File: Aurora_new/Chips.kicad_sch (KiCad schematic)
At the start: 89 parts, among them J1 UJ20-C-H-C-3-SMT-TR, J16 PPPC042LFBN-RC, J3 PPPC042LFBN-RC, J36 PPPC042LFBN-RC, J41 STEMMA QT, J6 DM3AT-SF-PEJM5, U1 STM32H757BITx, U13 XBP9X-DMUS-001, U14 MS5611-01BA, U2 USBLC6-2SC6, U3 TPS2121RUXR, U4 AP63203QWU-7, U5 ICM-45686, U6 ICM-42688-P, U7 BNO085, U9 MCP23017T-E_SO

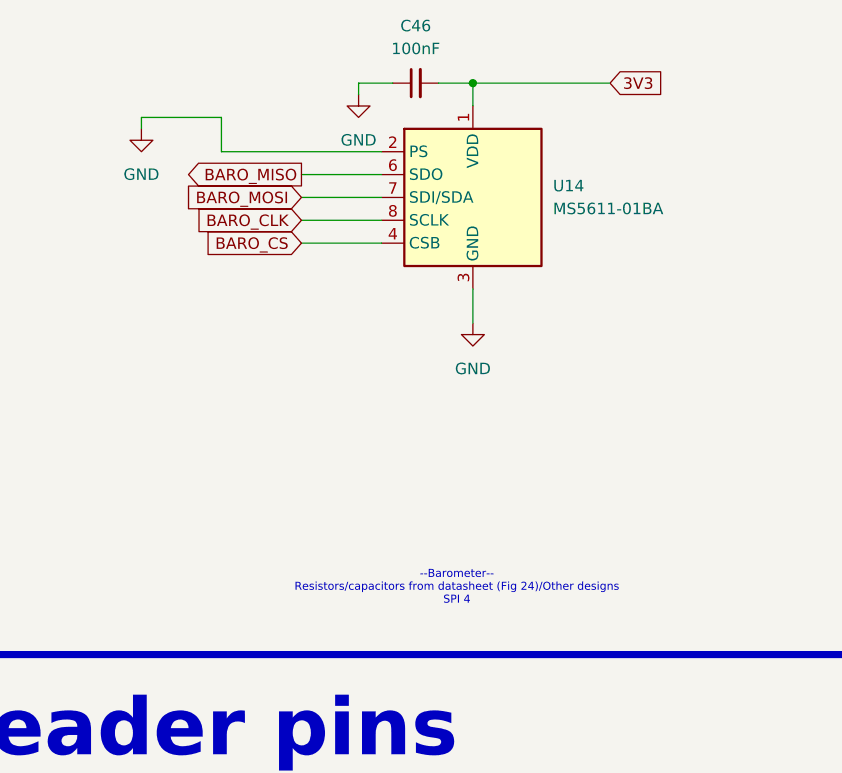
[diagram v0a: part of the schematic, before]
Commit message: PU resistor on CS for baro
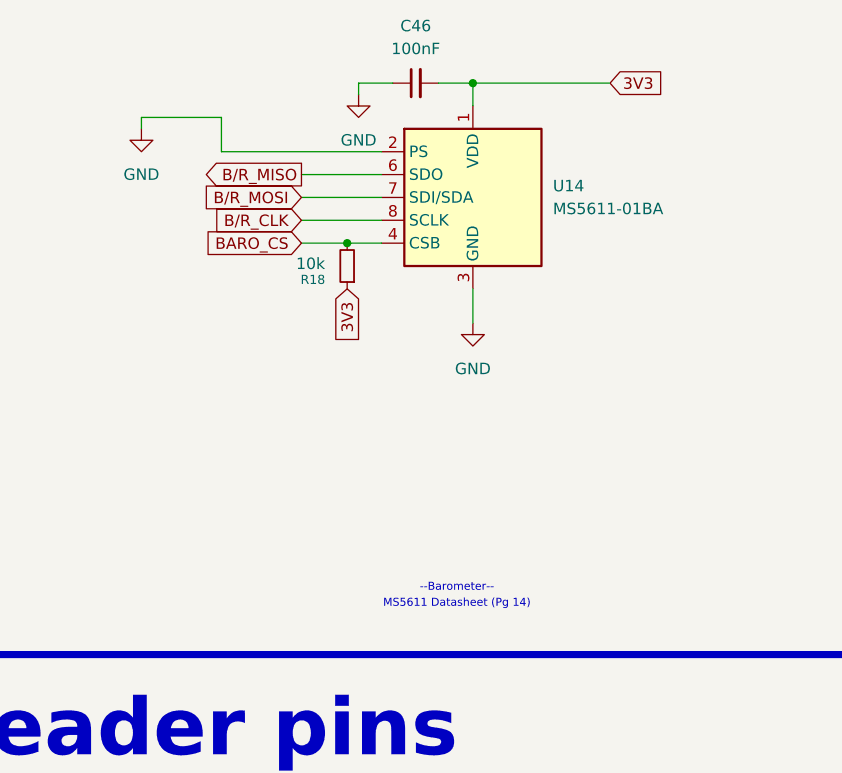
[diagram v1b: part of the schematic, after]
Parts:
- added R18: 10k, Resistor_SMD:R_0805_2012Metric, symbol Device:R_Small
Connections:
- net BARO_CLK is gone; now on net B/R_CLK: U14.8 (SCLK)
- net BARO_MISO is gone; now on net B/R_MISO: U14.6 (SDO)
- net BARO_MOSI is gone; now on net B/R_MOSI: U14.7 (SDI/SDA)
- net 3V3: now also R18.1
- net BARO_CS: now also R18.2
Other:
- note added: "--Barometer--"
- note added: "MS5611 Datasheet (Pg 14)"
- note removed: "--Barometer-- Resistors/capacitors from datasheet (Fig 24)/Other designs SPI 4"
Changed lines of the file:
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@@
 		)
 	)
-	(text "--Barometer--\nResistors/capacitors from datasheet (Fig 24)/Other designs\nSPI 4"
+	(text "--Barometer--"
 		(exclude_from_sim no)
 		(at 398.272 298.704 0)
@@
 		)
 	)
+	(text "MS5611 Datasheet (Pg 14)"
+		(exclude_from_sim no)
+		(at 398.272 300.482 0)
+		(effects
+			(font
+				(size 0.889 0.889)
+				(color 255 153 0 1)
+			)
+			(href "https://www.te.com/commerce/DocumentDelivery/DDEController?Action=srchrtrv&DocNm=MS5611-01BA03&DocType=Data%20Sheet&DocLang=English&DocFormat=pdf&PartCntxt=MS561101BA03-50")
+		)
+	)
 	(text "--USB Connector--\n+/- Diff pairs connected bc of usb-c symmetry\nVBUS pulled from device connected to voltage reg (5->3.3)\nCCs set up as a sink device to pull power from connection\nAll lines hooked up to ESD protection"
 		(exclude_from_sim no)
@@
 	)
 	(junction
+		(at 386.08 260.35)
+		(diameter 0)
+		(color 0 0 0 0)
+	)
+	(junction
 		(at 501.65 165.1)
 		(diameter 0)
@@
 	(wire
 		(pts
+			(xy 386.08 260.35) (xy 389.89 260.35)
+		)
+		(stroke
+			(width 0)
+			(type default)
+		)
+	)
+	(wire
+		(pts
 			(xy 182.88 143.51) (xy 180.34 143.51)
 		)
@@
 	(wire
 		(pts
-			(xy 381 260.35) (xy 389.89 260.35)
+			(xy 381 260.35) (xy 386.08 260.35)
 		)
 		(stroke
@@
 		)
 	)
-	(global_label "BARO_MOSI"
+	(global_label "B{slash}R_MOSI"
 		(shape input)
 		(at 381 255.27 180)
@@
 		)
 		(property "Intersheetrefs" "${INTERSHEET_REFS}"
-			(at 367.4919 255.27 0)
+			(at 368.5805 255.27 0)
 			(effects
 				(font
@@
 		)
 	)
-	(global_label "BARO_MISO"
+	(global_label "B{slash}R_MISO"
 		(shape output)
 		(at 381 252.73 180)
@@
 		)
 		(property "Intersheetrefs" "${INTERSHEET_REFS}"
-			(at 367.4919 252.73 0)
+			(at 368.5805 252.73 0)
 			(effects
 				(font
@@
 		)
 	)
-	(global_label "BARO_CLK"
+	(global_label "B{slash}R_CLK"
 		(shape input)
 		(at 381 257.81 180)
@@
 		)
 		(property "Intersheetrefs" "${INTERSHEET_REFS}"
-			(at 368.52 257.81 0)
+			(at 369.6086 257.81 0)
 			(effects
 				(font
@@
 		)
 	)
+	(global_label "3V3"
+		(shape input)
+		(at 386.08 265.43 270)
+		(fields_autoplaced yes)
+		(effects
+			(font
+				(size 1.27 1.27)
+			)
+			(justify right)
+		)
+		(property "Intersheetrefs" "${INTERSHEET_REFS}"
+			(at 386.08 271.9228 90)
+			(effects
+				(font
+					(size 1.27 1.27)
+				)
+				(justify right)
+				(hide yes)
+			)
+		)
+	)
 	(global_label "ADC2_SCL"
 		(shape input)
@@
 					(unit 1)
 				)
+			)
+		)
+	)
+	(symbol
+		(lib_id "Device:R_Small")
+		(at 386.08 262.89 180)
+		(unit 1)
+		(exclude_from_sim no)
+		(in_bom yes)
+		(on_board yes)
+		(dnp no)
+		(property "Reference" "R18"
+			(at 382.27 264.414 0)
+			(effects
+				(font
+					(size 1.016 1.016)
+				)
+			)
+		)
+		(property "Value" "10k"
+			(at 382.016 262.636 0)
+			(effects
+				(font
+					(size 1.27 1.27)
+				)
+			)
+		)
+		(property "Footprint" "Resistor_SMD:R_0805_2012Metric"
+			(at 386.08 262.89 0)
+			(effects
+				(font
+					(size 1.27 1.27)
+				)
+				(hide yes)
+			)
+		)
+		(property "Datasheet" "~"
+			(at 386.08 262.89 0)
+			(effects
+				(font
+					(size 1.27 1.27)
+				)
+				(hide yes)
+			)
+		)
+		(property "Description" "Resistor, small symbol"
+			(at 386.08 262.89 0)
+			(effects
+				(font
+					(size 1.27 1.27)
+				)
+				(hide yes)
+			)
+		)
+		(pin "2"
+		)
+		(pin "1"
+		)
+		(instances
+			(project "Aurora"
+				(path "/073f53a3-faa8-4419-bff2-f325850469a4/4a7b3f92-b695-4002-a887-607ce282d6cd"
+					(reference "R18")
+					(unit 1)
+				)

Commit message: added new regulator chain + rationale
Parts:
- removed C30: 10uF, Capacitor_SMD:C_0805_2012Metric, symbol Device:C_Small
- removed C31, C32: 22uF, Capacitor_SMD:C_0805_2012Metric, symbol Device:C_Small
- removed C33: 100uF, Capacitor_SMD:C_0805_2012Metric, symbol Device:C_Small
- removed L1: 3.3uH, Inductor_SMD:L_0805_2012Metric, symbol Device:L
- removed U4: AP63203QWU-7, TSOT26_DIO, symbol 2025-09-13_20-10-09:AP63203QWU-7
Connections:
- net 3V3: no longer C1.1, C10.1, C11.1, C12.1, C13.1, C14.1, C15.1, C16.1, C17.1, C18.1, C19.1, C2.1, C20.1, C21.1, C25.1, C26.1, C3.1, C34.1, C37.1, C38.2, C39.2, C4.1, C43.2, C44.1, C45.2, C46.2, C48.2, C49.2, C5.1, C50.2, C6.1, C60.1, C7.1, C8.1, C9.1, J6.4 (VDD), R11.1, U1.100 (VDD), U1.108 (VDD), U1.114 (VDD), U1.117 (VDD), U1.133 (VDD), U1.140 (VDD50_USB), U1.141 (VDD33_USB), U1.155 (VDD), U1.161 (VDD), U1.17 (VDD), U1.179 (VDD), U1.187 (VDD), U1.201 (PDR_ON), U1.208 (VDD), U1.29 (VDD), U1.43 (VREF+), U1.44 (VDDA), U1.49 (VDD), U1.56 (VDD), U1.7 (VDD), U1.74 (VDD), U1.8 (VBAT), U1.80 (VDD), U13.2 (VCC), U14.1 (VDD), U5.8 (VDD), U6.5 (VDDIO), U6.8 (VDD), U7.28 (VDDIO), U7.3 (VDD)
- new net 3V3_MCU: C1.1, C10.1, C11.1, C12.1, C13.1, C14.1, C15.1, C16.1, C17.1, C18.1, C19.1, C2.1, C20.1, C21.1, C25.1, C26.1, C3.1, C34.1, C4.1, C5.1, C6.1, C60.1, C7.1, C8.1, C9.1, U1.100 (VDD), U1.108 (VDD), U1.114 (VDD), U1.117 (VDD), U1.133 (VDD), U1.140 (VDD50_USB), U1.141 (VDD33_USB), U1.155 (VDD), U1.161 (VDD), U1.17 (VDD), U1.179 (VDD), U1.187 (VDD), U1.201 (PDR_ON), U1.208 (VDD), U1.29 (VDD), U1.43 (VREF+), U1.44 (VDDA), U1.49 (VDD), U1.56 (VDD), U1.7 (VDD), U1.74 (VDD), U1.8 (VBAT), U1.80 (VDD)
- new net 3V3_SENS: C37.1, C38.2, C39.2, C43.2, C44.1, C45.2, C46.2, J6.4 (VDD), R11.1, U14.1 (VDD), U5.8 (VDD), U6.5 (VDDIO), U6.8 (VDD), U7.28 (VDDIO), U7.3 (VDD)
- new net 3V3_XB: C48.2, C49.2, C50.2, U13.2 (VCC)
- no-connect marks 27 -> 28
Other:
- added sheet Regulators (untitled.kicad_sch)
- note added: "Regulators"
- note removed: "--3.3V Regulator-- Takes in output from Power MUX and regulates it down to 3.3V All wiring and resistor/capacitor values taken from datasheet"
- note removed: "3V3 Regulator"
